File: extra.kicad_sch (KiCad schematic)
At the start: 0 parts

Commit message: Digital IO, Relay, and Switchbox changes
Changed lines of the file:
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@@
+		)
+	)
+	(hierarchical_label "GasPedal"
+		(shape output)
+		(at 194.31 128.27 0)
+		(effects
+			(font
+				(size 2.54 2.54)
+			)
+			(justify left)
 		)
 	)

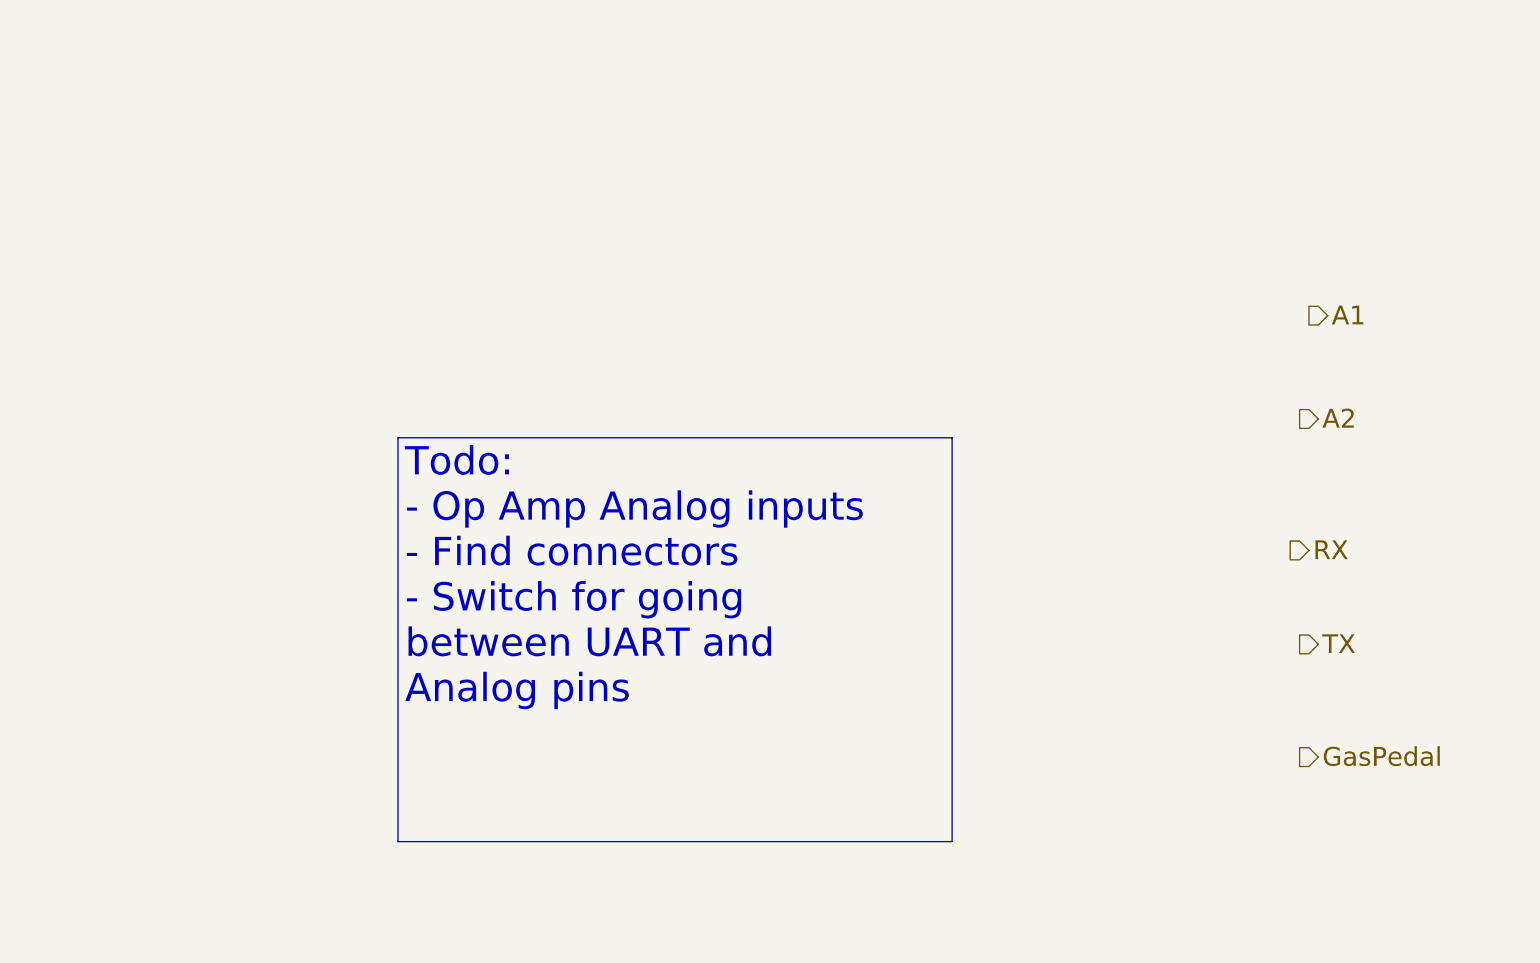
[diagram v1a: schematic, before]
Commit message: Added Analog inputs
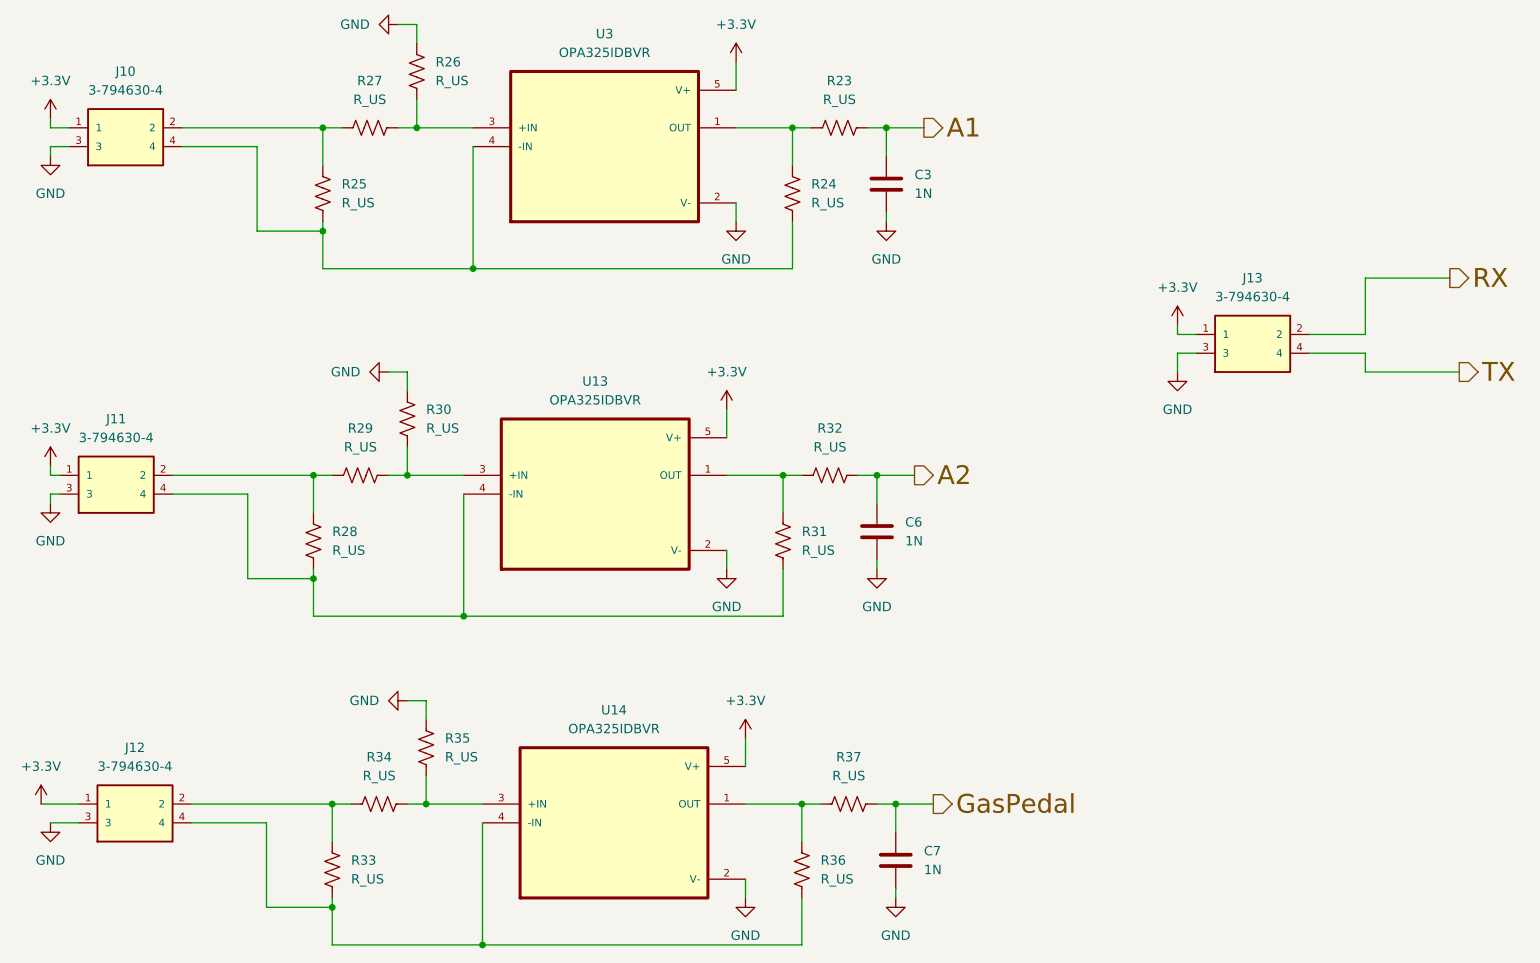
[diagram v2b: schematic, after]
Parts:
- added C3, C6, C7: 1N, symbol Device:C
- added J10, J11, J12, J13: 3-794630-4, 3-794630-4:CONN_3-794630-4, symbol 3-794630-4:3-794630-4
- added R23, R24, R25, R26, R27, R28, R29, R30, R31, R32, R33, R34, R35, R36, R37: R_US, symbol Device:R_US
- added U13, U14, U3: OPA325IDBVR, OPA325IDBVR:SOT95P280X145-5N, symbol OPA325IDBVR:OPA325IDBVR
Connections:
- net A1: now also C3.1, R23.2
- net A2: now also C6.1, R32.2
- net GasPedal: now also C7.1, R37.2
- net RX: now also J13.2
- net TX: now also J13.4
- new net: R31.2, R32.1, U13.1 (OUT)
- new net: R29.2, R30.2, U13.3 (+IN)
- new net: J11.4, R28.2, R31.1, U13.4 (-IN)
- new net: R36.2, R37.1, U14.1 (OUT)
- new net: J12.2, R33.1, R34.1
- new net: J12.4, R33.2, R36.1, U14.4 (-IN)
- new net: R34.2, R35.2, U14.3 (+IN)
- new net: R26.2, R27.2, U3.3 (+IN)
- new net: R23.1, R24.2, U3.1 (OUT)
- new net: J11.2, R28.1, R29.1
- new net: J10.2, R25.1, R27.1
- new net: J10.4, R24.1, R25.2, U3.4 (-IN)
- new net +3.3V: J10.1, J11.1, J12.1, J13.1, U13.5 (V+), U14.5 (V+), U3.5 (V+)
- new net GND: C3.2, C6.2, C7.2, J10.3, J11.3, J12.3, J13.3, R26.1, R30.1, R35.1, U13.2 (V-), U14.2 (V-), U3.2 (V-)
